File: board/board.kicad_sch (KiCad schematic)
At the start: 42 parts, among them J1 001_I2C, J2 019_100BASE-T_with_CT, J3 019_100BASE-T_with_CT, J4 019_100BASE-T_with_CT, J5 019_100BASE-T_with_CT, J6 019_100BASE-T_with_CT, J7 019_100BASE-T_with_CT, J8 019_100BASE-T_with_CT, J9 019_100BASE-T_with_CT

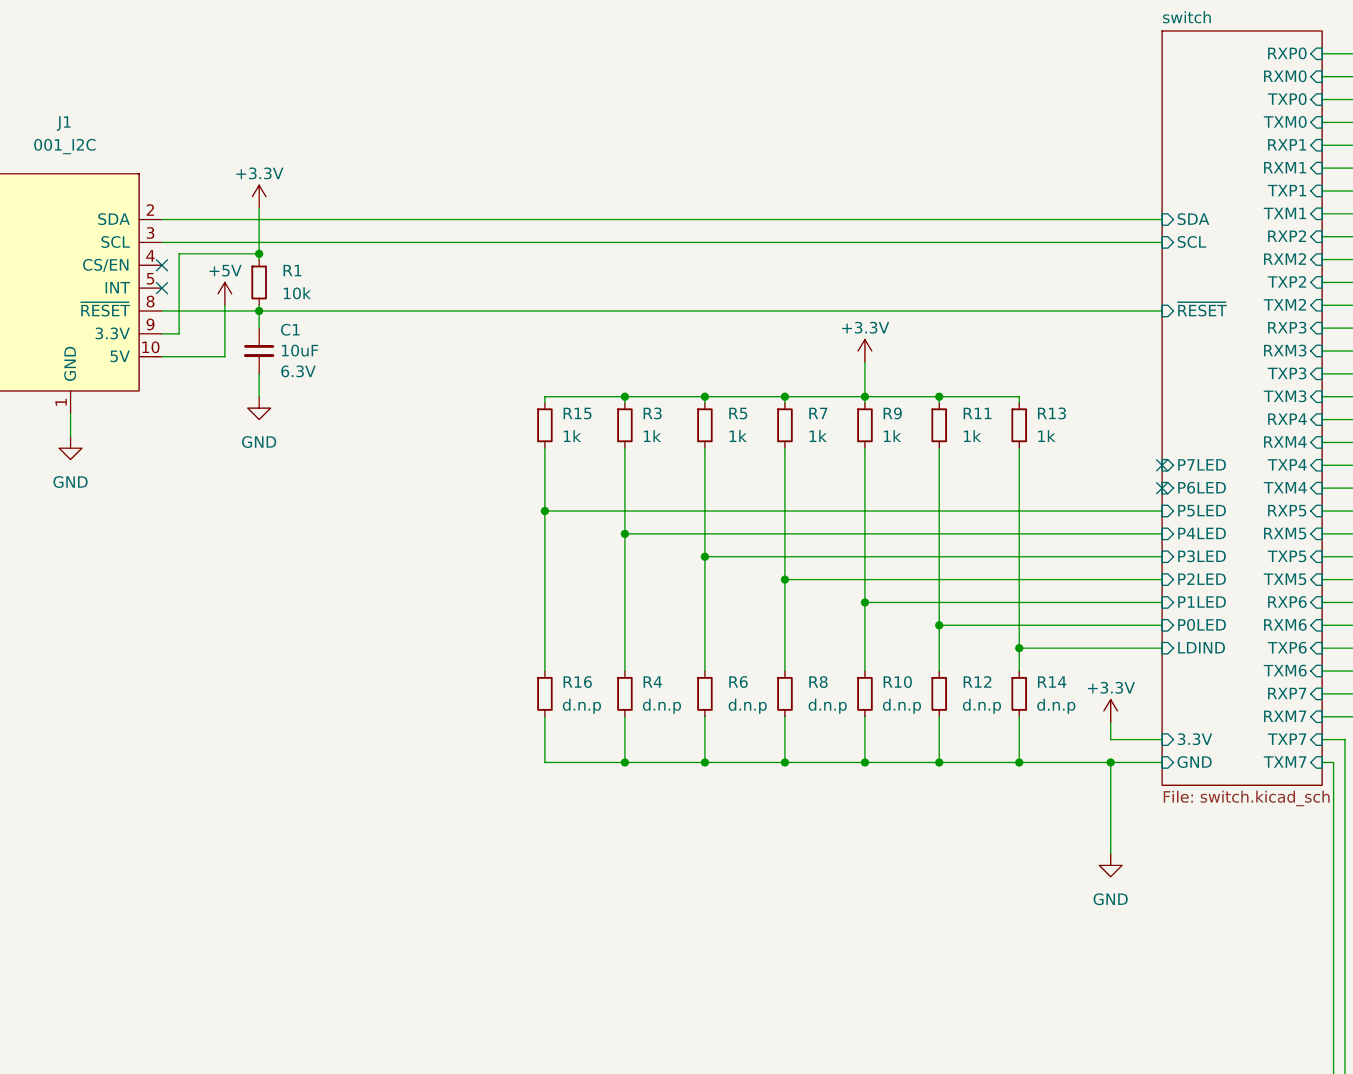
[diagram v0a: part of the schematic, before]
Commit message: added N filter for input voltage
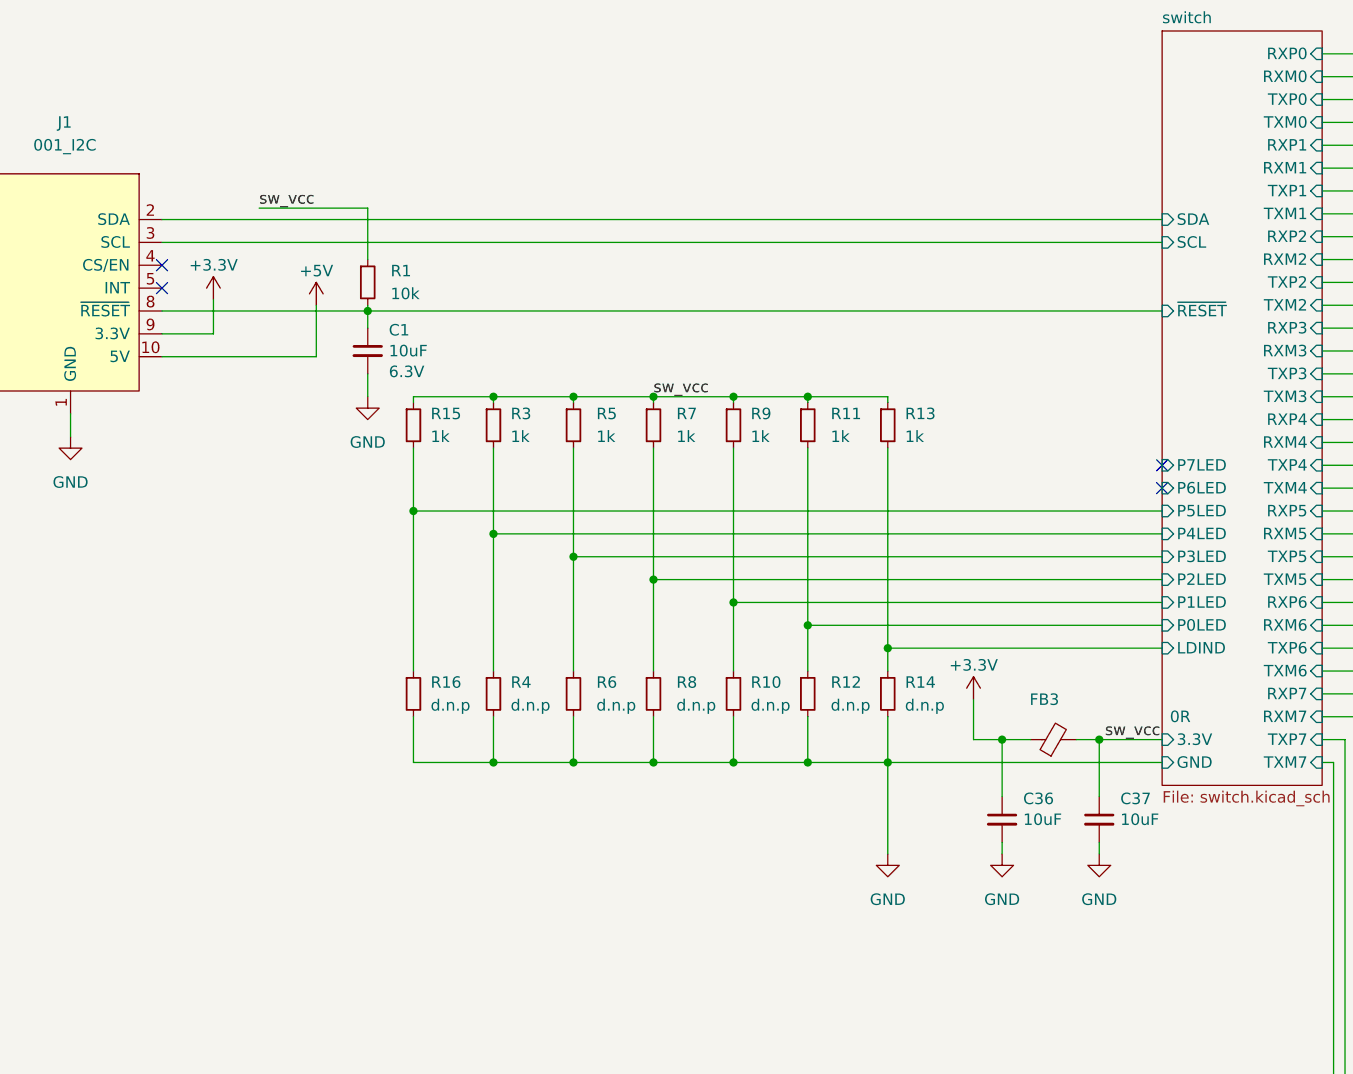
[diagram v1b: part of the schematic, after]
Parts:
- added C36, C37: 10uF, Capacitor_SMD:C_0603_1608Metric, symbol Device:C_Small
- added FB3: 0R, Inductor_SMD:L_0603_1608Metric, symbol Device:FerriteBead_Small
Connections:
- net +3.3V: now also C36.1, FB3.1; no longer R1.1, R11.1, R13.1, R15.1, R3.1, R5.1, R7.1, R9.1
- net GND: now also C36.2, C37.2
- new net sw_vcc: C37.1, FB3.2, R1.1, R11.1, R13.1, R15.1, R3.1, R5.1, R7.1, R9.1
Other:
- moved on the sheet: C1, R1, R10, R11, R12, R13, R14, R15, R16, R3, R4, R5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

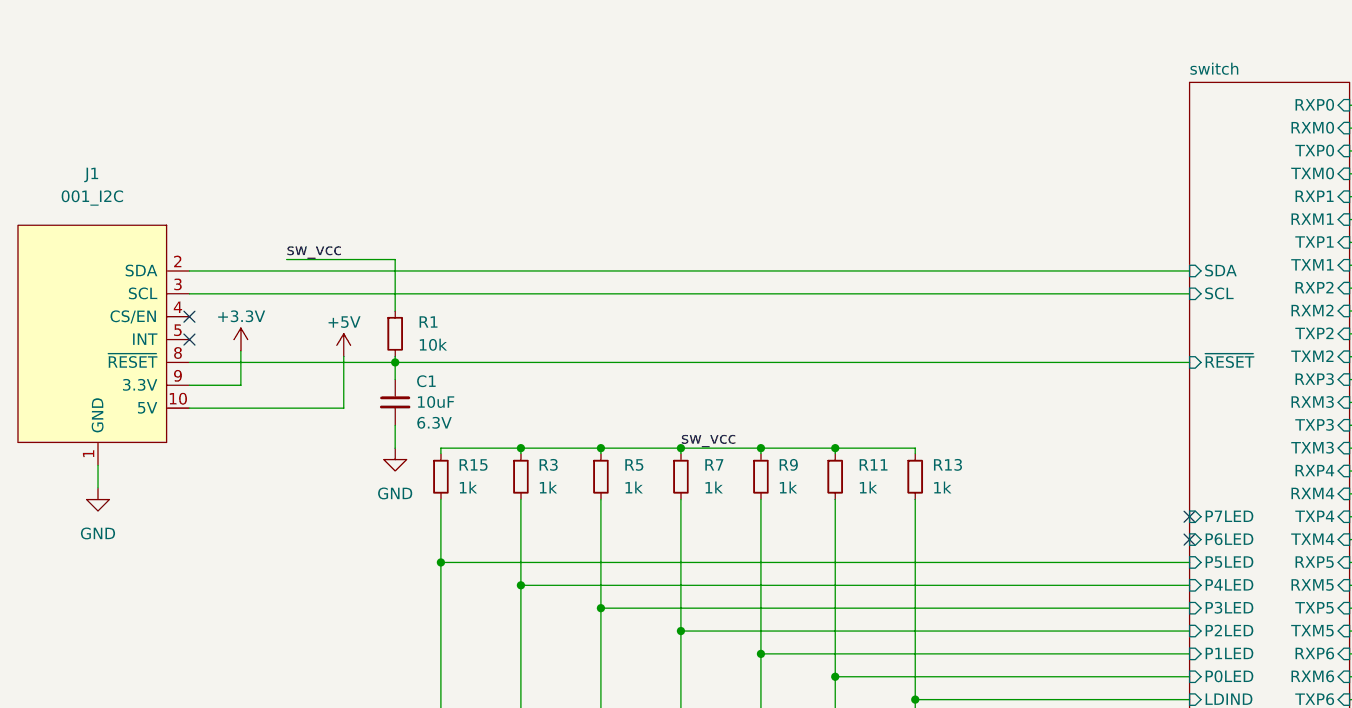
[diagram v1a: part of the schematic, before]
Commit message: added lcsc numbers and updated I2C connector
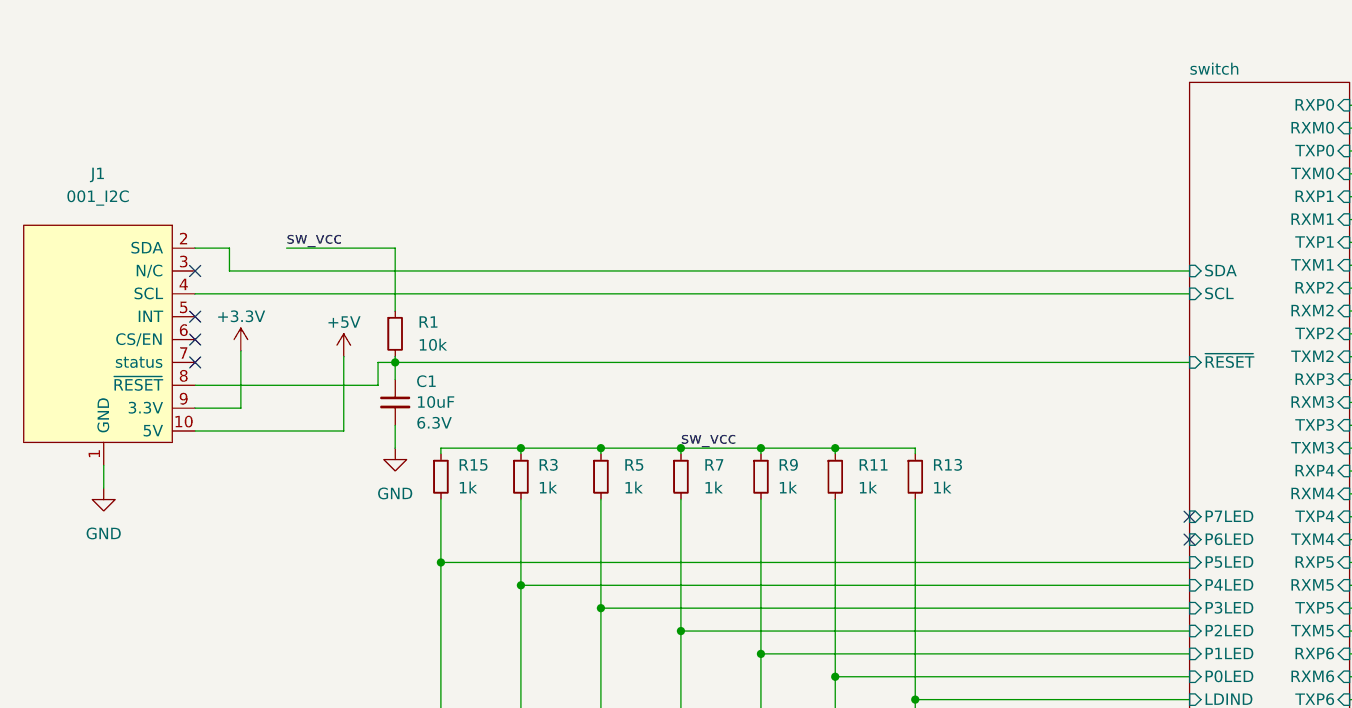
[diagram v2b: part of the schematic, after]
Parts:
- C1: lcsc (none) -> C15525
- C20, C21, C22, C23, C24, C25, C26, C27, C28, C29, C30, C31, C32, C33, C34, C35: lcsc (none) -> C14663
- C36, C37: footprint Capacitor_SMD:C_0603_1608Metric -> Capacitor_SMD:C_0402_1005Metric; lcsc (none) -> C15525
- FB3: lcsc (none) -> C21189
- R1: footprint Resistor_SMD:R_0603_1608Metric -> Resistor_SMD:R_0402_1005Metric; lcsc (none) -> C25744
- R11, R13, R15, R3, R5, R7, R9: footprint Resistor_SMD:R_0603_1608Metric -> Resistor_SMD:R_0402_1005Metric; lcsc (none) -> C11702
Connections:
- net switch/SCL: now also J1.4 (SCL); no longer J1.3 (SCL)
- no-connect marks 4 -> 6
